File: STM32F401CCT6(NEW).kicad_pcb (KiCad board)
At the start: 2 copper layers, 52 x 22.9 mm, 37 parts, among them J1 USB_OTG, J2 Conn_02x03_Odd_Even, J3 Conn_01x20_des, J4 Conn_01x05_desc, J5 Conn_01x20, SW1 SW_Push, U1 MIC5219-3.3, U2 STM32F401CCT6, U3 USBLC6-2SC6, Y1 32.786K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

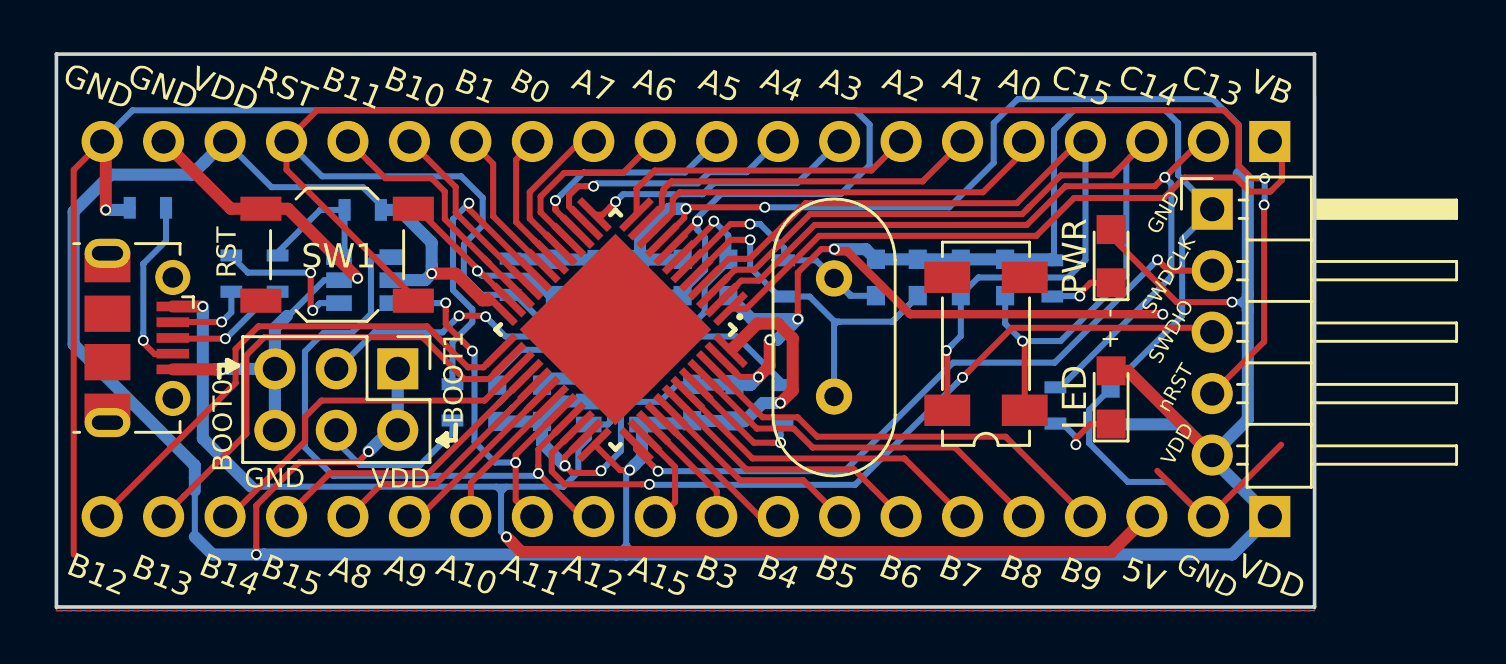
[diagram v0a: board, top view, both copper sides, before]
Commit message: Updated the via diamter and drill size 0.435/0.3 mm
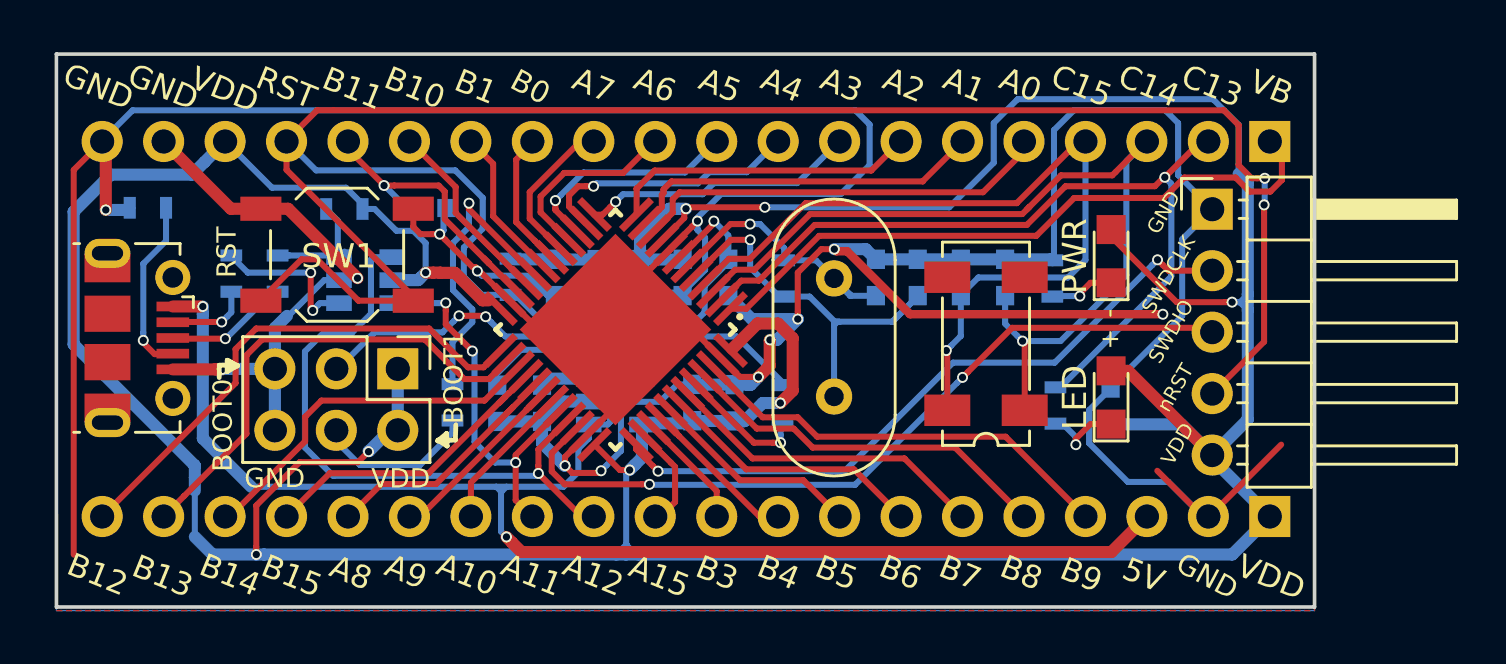
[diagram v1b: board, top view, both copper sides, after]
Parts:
- added 4.7u,0603: C, Capacitors_SMD:C_0603, B.Cu at (89.1, 106.4)
- moved R10 0.76 mm to (85.6, 106.5)
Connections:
- J1 pad 6: (no net) -> Net-(J1-Pad6)
- U2 pad 0: (no net) -> GND
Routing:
- net GND: track 219.7 -> 240.4 mm, vias 12 -> 13
- net /RESET: track 91.7 -> 99.4 mm
- net /PB11: track 10.6 -> 12.2 mm, vias 0 -> 1
- net VCC: track 198.4 -> 197.8 mm
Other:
- net class Default: via_dia 0.6 -> 0.453; via_drill 0.4 -> 0.3
- net class new: via_dia 0.45 -> 0.453

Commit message: Re-routed (prioritised D+ D- SWDIO SWCLK) by reducing the track length and via along the tracks.
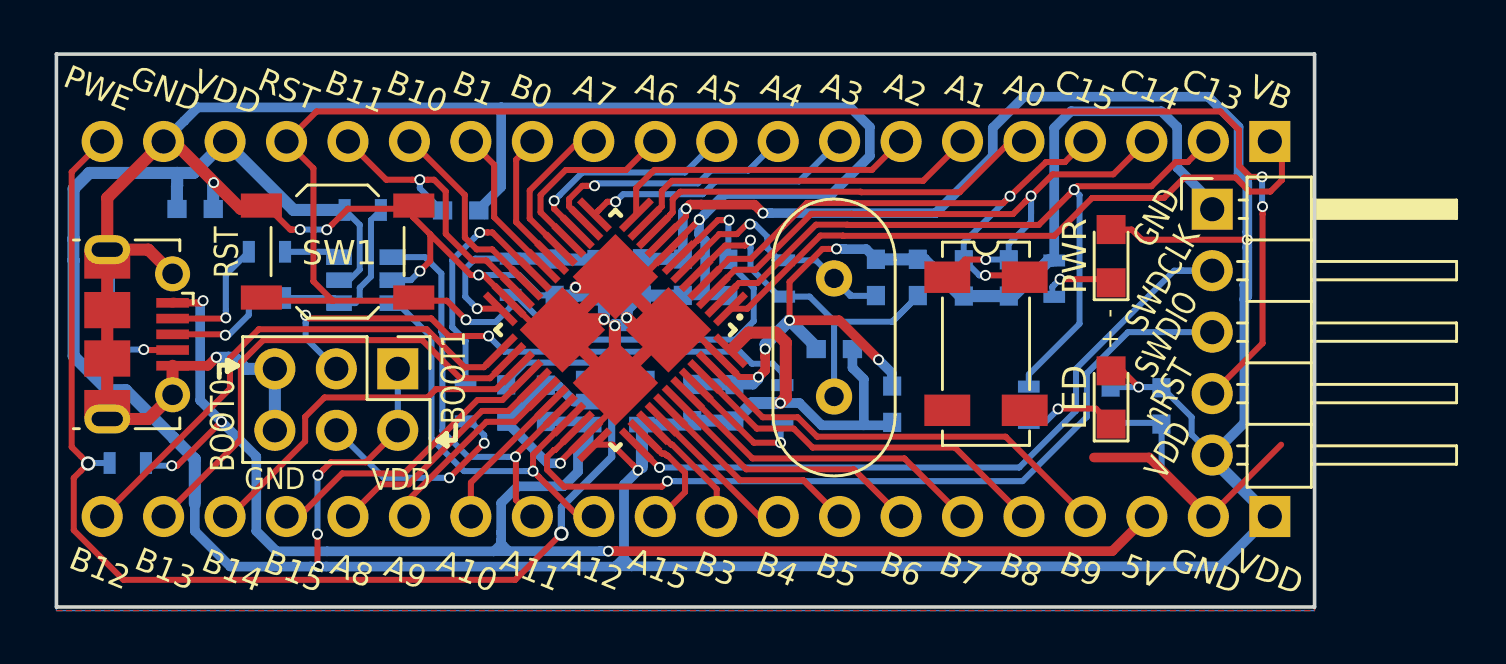
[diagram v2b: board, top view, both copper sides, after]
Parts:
- removed 4.7u,0603: C, Capacitors_SMD:C_0603
- added C15: 4.7u,0603, Capacitors_SMD:C_0603, B.Cu at (90.4, 106.5)
- added C16: 0.1uF,0603, Capacitors_SMD:C_0603, B.Cu at (79.5, 106.5)
- added C17: 104,0603, Capacitors_SMD:C_0603, B.Cu at (119.4, 114.6)
- added C18: 104,0603, Capacitors_SMD:C_0603, B.Cu at (108.3, 114.5)
- added C19: 0.1uF,0603, Capacitors_SMD:C_0603, B.Cu at (105.9, 112.2)
- added R11: 10K, Resistors_SMD:R_0603, B.Cu at (76.7, 117.0)
- C10, C11: value 104,0603 -> 4.7uF,0603
- moved R9 5.41 mm to (75.9, 111.6), turned to 270 degrees
- moved C11 5.29 mm to (94.3, 109.3)
- moved C12 3.60 mm to (97.9, 109.3)
- moved C10 1.77 mm to (99.6, 109.3)
- moved R3 1.72 mm to (82.4, 108.2), turned to 180 degrees
- moved R4 1.10 mm to (82.4, 110.1), turned to 180 degrees
- moved R6 1.10 mm to (113.9, 114.5)
- moved R10 0.76 mm to (86.4, 106.5), turned to 180 degrees
- moved R8 0.54 mm to (90.6, 114.5)
- moved C2 0.37 mm to (92.3, 114.5)
- moved C1 0.16 mm to (94.0, 114.5), turned to 90 degrees
- moved C6 0.15 mm to (113.1, 109.3), turned to 270 degrees
- moved J1 0.15 mm to (76.2, 111.6)
- moved SW1 0.13 mm to (85.3, 108.2)
- moved C7 0.12 mm to (111.2, 109.3), turned to 270 degrees
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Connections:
- net /PB11 renamed /PB11/VCAP1
- J1 pad 6: Net-(J1-Pad6) -> GND
- J3 pad 20: GND -> /PWR_EN
- U1 pad 3: +5V -> /PWR_EN
- U3 pad 1: Net-(R3-Pad1) -> /PA11
- U3 pad 3: Net-(R10-Pad1) -> /PA12
- U3 pad 4: /PA12 -> Net-(R10-Pad1)
- U3 pad 6: /PA11 -> Net-(R3-Pad1)
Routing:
- net /PWR_EN: track 0.00 -> 48.0 mm, vias 0 -> 2
- net /PC14: track 37.4 -> 26.6 mm, vias 1 -> 2
- net GND: track 240.4 -> 229.9 mm, vias 13 -> 17
- net /PA12: track 26.8 -> 17.5 mm
- net /PC15: track 33.9 -> 24.7 mm, vias 1 -> 2
- net /RESET: track 99.4 -> 90.5 mm, vias 3 -> 4
- net +5V: track 61.3 -> 66.8 mm, vias 2 -> 4
- net /ID: track 7.83 -> 2.69 mm
- net Net-(R3-Pad1): track 6.40 -> 2.32 mm, vias 2 -> 0
- net VCC: track 197.8 -> 201.4 mm, vias 8 -> 10
- net Net-(J2-Pad3): track 20.6 -> 24.0 mm
- net /BOOT1: track 12.5 -> 10.00 mm
- net Net-(J2-Pad4): track 6.64 -> 8.85 mm, vias 0 -> 2
- net /D-: track 3.48 -> 5.34 mm
- net /PA11: track 15.9 -> 17.8 mm, vias 3 -> 1
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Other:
- net class Default: via_dia 0.453 -> 0.6; via_drill 0.3 -> 0.4
- board text added: "PWE"
